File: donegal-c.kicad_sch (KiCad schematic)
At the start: 181 parts, among them J2 ISP, SW1 SW_SPST, SW10 SW_SPST, SW11 SW_SPST, SW12 SW_SPST, SW13 SW_SPST, SW14 SW_SPST, SW15 SW_SPST, SW16 SW_SPST, SW17 SW_SPST, SW18 SW_SPST, SW19 SW_SPST, SW2 SW_SPST, SW20 SW_SPST, SW21 SW_SPST, SW22 SW_SPST, SW23 SW_SPST, SW24 SW_SPST, SW25 SW_SPST, SW26 SW_SPST, SW27 SW_SPST, SW28 SW_SPST, SW29 SW_SPST, SW3 SW_SPST, SW30 SW_SPST, SW31 SW_SPST, SW32 SW_SPST, SW33 SW_SPST, SW34 SW_SPST, SW35 SW_SPST, SW36 SW_SPST, SW37 SW_SPST, SW38 SW_SPST, SW39 SW_SPST, SW4 SW_SPST, SW40 SW_SPST, SW41 SW_SPST, SW42 SW_SPST, SW43 SW_SPST, SW44 SW_SPST, SW45 SW_SPST, SW46 SW_SPST, SW47 SW_SPST, SW48 SW_SPST, SW49 SW_SPST, SW5 SW_SPST, SW50 SW_SPST, SW51 SW_SPST, SW52 SW_SPST, SW53 SW_SPST, SW54 SW_SPST, SW55 SW_SPST, SW56 SW_SPST, SW57 SW_SPST, SW58 SW_SPST, SW59 SW_SPST, SW6 SW_SPST, SW60 SW_SPST, SW61 SW_SPST, SW62 SW_SPST, SW63 SW_SPST, SW64 SW_SPST, SW65 SW_SPST, SW66 SW_SPST, SW67 SW_SPST, SW68 RESET, SW69 BOOT, SW7 SW_SPST, SW70 SW_SPST, SW71 SW_SPST, SW72 SW_SPST, SW73 SW_SPST, SW74 SW_SPST, SW75 SW_SPST, SW76 SW_SPST, SW77 SW_SPST, SW78 SW_SPST, SW79 SW_SPST, SW8 SW_SPST, SW80 SW_SPST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

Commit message: removed unneeded files and replaced others
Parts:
- removed SW15, SW29, SW47, SW58, SW59, SW71, SW74, SW77: SW_SPST, MX_Only:MXOnly-1U-NoLED, symbol Switch:SW_SPST
- removed SW43, SW73, SW75, SW78, SW79: SW_SPST, MX_Only:MXOnly-1.5U-NoLED, symbol Switch:SW_SPST
- removed SW44: SW_SPST, MX_Only:MXOnly-2.25U-NoLED, symbol Switch:SW_SPST
- removed SW63: SW_SPST, MX_Only:MXOnly-6.25U-ReversedStabilizers-NoLED, symbol Switch:SW_SPST
- removed SW70, SW72, SW81: SW_SPST, MX_Only:MXOnly-1.25U-NoLED, symbol Switch:SW_SPST
- H1, H2: footprint MountingHole:MountingHole_2.2mm_M2_DIN965_Pad -> MountingHole:MountingHole_2.2mm_M2
- H10, H3, H4, H6, H7, H8, H9: now left out of the parts list
- H5: footprint MountingHole:MountingHole_2.2mm_M2_DIN965_Pad -> MountingHole:MountingHole_2.2mm_M2_DIN965; now left out of the parts list
- SW1: footprint MX_Only:MXOnly-2U-NoLED -> Alps_Only:ALPS-1.5U
- SW10, SW11, SW12, SW13, SW14, SW17, SW18, SW19, SW2, SW20, SW21, SW22, SW23, SW24, SW25, SW26, SW27, SW28, SW3, SW32, SW33, SW34, SW35, SW36, SW37, SW38, SW39, SW4, SW40, SW41, SW42, SW48, SW49, SW5, SW50, SW51, SW52, SW53, SW54, SW55, SW56, SW57, SW6, SW7, SW8, SW9: footprint MX_Only:MXOnly-1U-NoLED -> Alps_Only:ALPS-1U
- SW16: footprint MX_Only:MXOnly-1.5U-NoLED -> Alps_Only:ALPS-1.5U
- SW30: footprint MX_Only:MXOnly-ISO-ROTATED-ReversedStabilizers-NoLED -> Alps_Only:ALPS-2U
- SW31: footprint MX_Only:MXOnly-1.75U-NoLED -> Alps_Only:ALPS-1.75U
- SW45: footprint MX_Only:MXOnly-2.75U-NoLED -> Alps_Only:ALPS-2.25U
- SW46: footprint MX_Only:MXOnly-2.25U-NoLED -> Alps_Only:ALPS-2.25U
- SW60, SW61, SW64, SW65, SW66, SW67: footprint MX_Only:MXOnly-1.25U-NoLED -> Alps_Only:ALPS-1U
- SW62: footprint MX_Only:MXOnly-1.25U-NoLED -> Alps_Only:ALPS-1.75U
- SW76: footprint MX_Only:MXOnly-7U-ReversedStabilizers-NoLED -> Alps_Only:ALPS-2U
- SW80: footprint MX_Only:MXOnly-2.75U-ReversedStabilizers-NoLED -> Alps_Only:ALPS-1U
- SW82: footprint MX_Only:MXOnly-2.25U-ReversedStabilizers-NoLED -> Alps_Only:ALPS-1U
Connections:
- net GND: no longer H1.1, H10.1, H2.1, H3.1, H4.1, H5.1, H6.1, H7.1, H8.1, H9.1
- new net: H1.1, H2.1, H3.1, H4.1, H5.1
- new net: H10.1, H6.1, H7.1, H8.1, H9.1

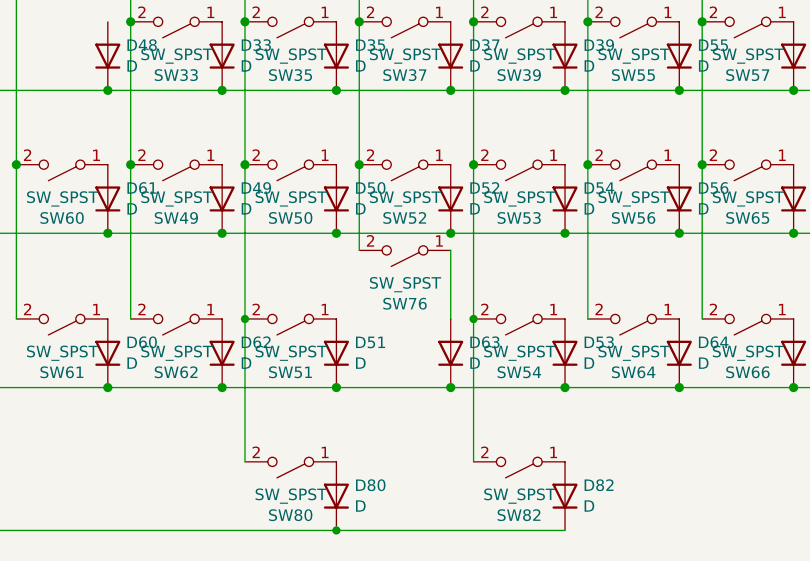
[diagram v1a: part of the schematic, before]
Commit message: changed spacebar to wider hole and moved some silk
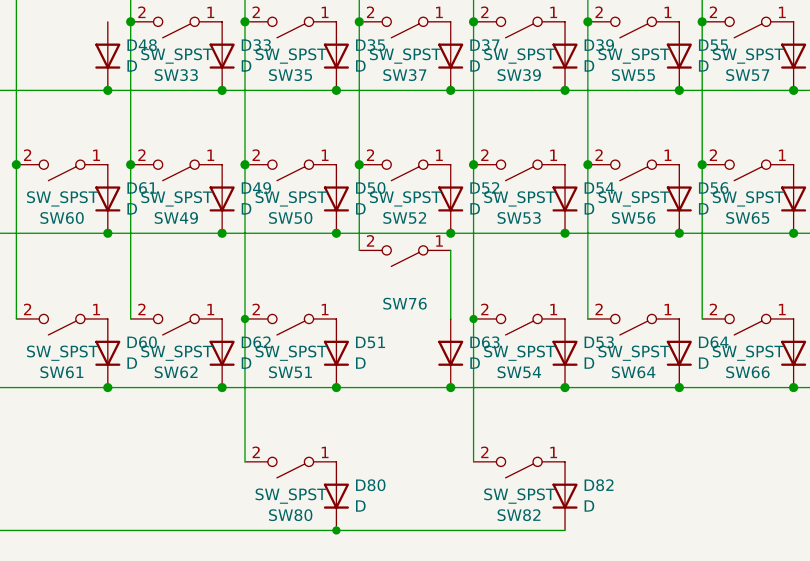
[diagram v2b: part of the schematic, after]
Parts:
- SW76: value SW_SPST -> (none); footprint Alps_Only:ALPS-2U -> (none)
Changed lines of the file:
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@@
     (in_bom yes) (on_board yes)
     (property "Reference" "SW76" (id 0) (at 70.485 170.434 0))
-    (property "Value" "SW_SPST" (id 1) (at 70.485 168.1226 0))
-    (property "Footprint" "Alps_Only:ALPS-2U" (id 2) (at 70.485 164.465 0)
+    (property "Value" "" (id 1) (at 70.485 168.1226 0))
+    (property "Footprint" "" (id 2) (at 70.485 164.465 0)
       (effects (font (size 1.27 1.27)) hide)
     )
@@
     )
     (path "/62926ecc-974f-49b7-a25d-42eee5b73239"
-      (reference "SW76") (unit 1) (value "SW_SPST") (footprint "Alps_Only:ALPS-2U")
+      (reference "SW76") (unit 1) (value "SW_SPST") (footprint "Alps_Only:ALPS-2.25U")
     )
     (path "/a69f5ac2-ec68-4655-8087-bfc4281d5652"
